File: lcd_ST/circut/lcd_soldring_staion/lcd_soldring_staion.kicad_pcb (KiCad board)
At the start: 2 copper layers, 41.7 x 41 mm, 35 parts, among them J2 Conn_01x05_Pin, J3 Conn_01x01_Pin, J4 Conn_01x01_Pin, J44 Screw_Terminal_01x02, J5 Conn_01x01_Pin, J6 Conn_01x01_Pin, J7 Conn_01x04_Pin, Q2 Si4162DY, SW1 SW_Push, U1 PIC16F15223T-I/SL, U2 L7805, U3 LM358

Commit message: done v0
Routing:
- net VPP: track 15.3 -> 15.8 mm

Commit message: V2_PCB EDITING
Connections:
- C4 pad 1: T+ -> T-
- C4 pad 2: T- -> T+
- C9 pad 1: c+ -> c-
- C9 pad 2: c- -> c+
- R10 pad 2: Net-(U3B--) -> Net-(U3B-+)
- R11 pad 1: Net-(U3B-+) -> Net-(U3B--)
- R2 pad 1: T+ -> T-
- R2 pad 2: Net-(U3A-+) -> Net-(U3A--)
- R3 pad 1: Net-(U3A-+) -> Net-(U3A--)
- R4 pad 1: T- -> T+
- R4 pad 2: Net-(U3A--) -> Net-(U3A-+)
- R5 pad 2: Net-(U3A--) -> Net-(U3A-+)
- R8 pad 1: c+ -> c-
- R8 pad 2: Net-(U3B-+) -> Net-(U3B--)
- R9 pad 1: c- -> c+
- R9 pad 2: Net-(U3B--) -> Net-(U3B-+)
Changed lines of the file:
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@@
 			(layers "B.Cu" "B.Mask" "B.Paste")
 			(roundrect_rratio 0.192308)
-			(net 19 "Net-(U3A--)")
+			(net 17 "Net-(U3A-+)")
 			(pintype "passive")
 		)
@@
 			(layers "B.Cu" "B.Mask" "B.Paste")
 			(roundrect_rratio 0.192308)
-			(net 5 "T-")
+			(net 6 "T+")
 			(pintype "passive")
 		)
@@
 			(layers "B.Cu" "B.Mask" "B.Paste")
 			(roundrect_rratio 0.192308)
-			(net 19 "Net-(U3A--)")
+			(net 17 "Net-(U3A-+)")
 			(pintype "passive")
 		)
@@
 			(layers "B.Cu" "B.Mask" "B.Paste")
 			(roundrect_rratio 0.192308)
-			(net 2 "c-")
+			(net 9 "c+")
 			(pintype "passive")
 		)
@@
 			(layers "B.Cu" "B.Mask" "B.Paste")
 			(roundrect_rratio 0.192308)
-			(net 22 "Net-(U3B--)")
+			(net 21 "Net-(U3B-+)")
 			(pintype "passive")
 		)
@@
 			(layers "B.Cu" "B.Mask" "B.Paste")
 			(roundrect_rratio 0.192308)
-			(net 6 "T+")
+			(net 5 "T-")
 			(pintype "passive")
 		)
@@
 			(layers "B.Cu" "B.Mask" "B.Paste")
 			(roundrect_rratio 0.192308)
-			(net 17 "Net-(U3A-+)")
+			(net 19 "Net-(U3A--)")
 			(pintype "passive")
 		)
@@
 			(layers "B.Cu" "B.Mask" "B.Paste")
 			(roundrect_rratio 0.192308)
-			(net 17 "Net-(U3A-+)")
+			(net 19 "Net-(U3A--)")
 			(pintype "passive")
 		)
@@
 			(layers "B.Cu" "B.Mask" "B.Paste")
 			(roundrect_rratio 0.188679)
-			(net 9 "c+")
+			(net 2 "c-")
 			(pintype "passive")
 		)
@@
 			(layers "B.Cu" "B.Mask" "B.Paste")
 			(roundrect_rratio 0.188679)
-			(net 2 "c-")
+			(net 9 "c+")
 			(pintype "passive")
 		)
@@
 			(layers "B.Cu" "B.Mask" "B.Paste")
 			(roundrect_rratio 0.192308)
-			(net 21 "Net-(U3B-+)")
+			(net 22 "Net-(U3B--)")
 			(pintype "passive")
 		)
@@
 			(layers "B.Cu" "B.Mask" "B.Paste")
 			(roundrect_rratio 0.192308)
-			(net 22 "Net-(U3B--)")
+			(net 21 "Net-(U3B-+)")
 			(pintype "passive")
 		)
@@
 			(layers "B.Cu" "B.Mask" "B.Paste")
 			(roundrect_rratio 0.188679)
-			(net 6 "T+")
+			(net 5 "T-")
 			(pintype "passive")
 		)
@@
 			(layers "B.Cu" "B.Mask" "B.Paste")
 			(roundrect_rratio 0.188679)
-			(net 5 "T-")
+			(net 6 "T+")
 			(pintype "passive")
 		)
@@
 			(layers "B.Cu" "B.Mask" "B.Paste")
 			(roundrect_rratio 0.192308)
-			(net 9 "c+")
+			(net 2 "c-")
 			(pintype "passive")
 		)
@@
 			(layers "B.Cu" "B.Mask" "B.Paste")
 			(roundrect_rratio 0.192308)
-			(net 21 "Net-(U3B-+)")
+			(net 22 "Net-(U3B--)")
 			(pintype "passive")
 		)

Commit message: pcb v2
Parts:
- added D1: LED, LED_SMD:LED_1210_3225Metric_Pad1.42x2.65mm_HandSolder, B.Cu at (119.4, 67.2)
- added J8: 01x04, Connector:01x04_fat_pins, F.Cu at (106.6, 64.1)
- added J9: Connector:01x04_fat_pins, Connector:01x04_fat_pins, F.Cu at (106.6, 72.1)
- added R14: 1K, Resistor_SMD:R_0805_2012Metric_Pad1.20x1.40mm_HandSolder, B.Cu at (120.1, 57.6)
- added R15: 1K, Resistor_SMD:R_0805_2012Metric_Pad1.20x1.40mm_HandSolder, B.Cu at (120.1, 60.6)
- added R16: 1K, Resistor_SMD:R_0805_2012Metric_Pad1.20x1.40mm_HandSolder, B.Cu at (120.1, 63.5)
- J7: footprint Connector:FanPinHeader_1x04_P2.54mm_Vertical -> Connector:01x04_fat_pins
- R1, R10, R11, R12, R2, R3, R4, R5, R6, R8, R9: footprint Resistor_SMD:R_1206_3216Metric_Pad1.30x1.75mm_HandSolder -> Resistor_SMD:R_0805_2012Metric_Pad1.20x1.40mm_HandSolder
- R13: footprint Resistor_SMD:R_1812_4532Metric_Pad1.30x3.40mm_HandSolder -> Resistor_SMD:R_0805_2012Metric_Pad1.20x1.40mm_HandSolder
- R7: value 1K -> 0.02
- moved J7 4.16 mm to (131.2, 82.8)
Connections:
- net PGC renamed B
- net PGD renamed A
- net temp_set renamed ClC
- U1 pad 11: unconnected-(U1-RA2-Pad11) -> TX
- U1 pad 6: unconnected-(U1-RC4-Pad6) -> Net-(U1-RC4)
- U1 pad 8: unconnected-(U1-RC2-Pad8) -> RX

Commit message: pcb v2
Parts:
- removed J9: Connector:01x04_fat_pins, Connector:01x04_fat_pins
- removed R15: 1K, Resistor_SMD:R_0805_2012Metric_Pad1.20x1.40mm_HandSolder
- removed RV1: R_Potentiometer, Potentiometer_THT:Potentiometer_ACP_CA9-H2,5_Horizontal
- J7: footprint Connector:01x04_fat_pins -> Connector:FanPinHeader_1x04_P2.54mm_Vertical
- J8: value 01x04 -> Conn_01x04_Pin; footprint Connector:01x04_fat_pins -> Connector:FanPinHeader_1x04_P2.54mm_Vertical
- R1: value 330 -> 50; footprint Resistor_SMD:R_0805_2012Metric_Pad1.20x1.40mm_HandSolder -> Resistor_THT:R_Axial_DIN0207_L6.3mm_D2.5mm_P7.62mm_Horizontal
- moved C5 11.9 mm to (153.4, 65.8), turned to 0 degrees
- moved R9 3.07 mm to (164.1, 82.8)
- moved R2 2.84 mm to (159.8, 62.9)
- moved R8 2.33 mm to (161.2, 82.8)
- moved R3 1.91 mm to (158.7, 66.2), turned to 180 degrees
- moved R4 1.90 mm to (162.0, 62.9)
- moved R5 0.63 mm to (162.8, 66.6)
- moved R6 0.59 mm to (157.5, 62.8)
- turned C4 to 0 degrees
- turned C9 to 0 degrees
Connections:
- D1 pad 1: c- -> unconnected-(D1-K-Pad1)
- R16 pad 2: Net-(U1-RC4) -> unconnected-(R16-Pad2)
- U1 pad 6: Net-(U1-RC4) -> unconnected-(U1-RC4-Pad6)
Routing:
- net c-: track 168.7 -> 125.5 mm
- net c+: track 17.6 -> 2.68 mm
- net TEMP: track 36.5 -> 27.3 mm
- net Net-(U3A-+): track 14.4 -> 5.82 mm
- net Net-(U3B-+): track 4.94 -> 10.7 mm
- net T-: track 5.47 -> 0.00 mm
- net T+: track 4.95 -> 0.00 mm
- net Net-(U3B--): track 10.6 -> 6.59 mm
- net heater: track 10.5 -> 8.59 mm
- net current: track 21.3 -> 22.5 mm
- net Net-(U3A--): track 5.27 -> 6.12 mm
- net Net-(R11-Pad2): track 5.40 -> 6.04 mm

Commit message: pcbing
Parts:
- removed J4: Conn_01x01_Pin, Connector_PinHeader_2.54mm:PinHeader_1x01_P2.54mm_Vertical
- removed R14: 1K, Resistor_SMD:R_0805_2012Metric_Pad1.20x1.40mm_HandSolder
- J7, J8: footprint Connector:FanPinHeader_1x04_P2.54mm_Vertical -> Connector:01x04_fat_pins
- U3: footprint Package_SO:SOIC-8_5.3x6.2mm_P1.27mm -> Package_SO:SOIC-8_3.9x4.9mm_P1.27mm
- moved J8 35.4 mm to (131.4, 89.2), turned to 90 degrees
- moved R1 4.90 mm to (145.9, 62.2)
- moved J7 3.90 mm to (131.4, 78.9)
- moved C6 1.76 mm to (152.3, 84.6)
- moved C1 1.47 mm to (136.0, 79.2), turned to -90 degrees
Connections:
- U1 pad 10: dat -> clk
- U1 pad 11: TX -> dat
- U1 pad 9: clk -> TX
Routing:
- net c-: track 125.5 -> 96.8 mm
- net VCC: track 66.8 -> 79.8 mm
- net RX: track 0.00 -> 11.8 mm
- net TX: track 0.00 -> 11.4 mm
- net +24V: track 17.2 -> 6.60 mm
- net Net-(U3B--): track 6.59 -> 7.62 mm
- net Net-(R11-Pad2): track 6.04 -> 7.06 mm
- net Net-(U3A--): track 6.12 -> 7.14 mm
- net Net-(U3A-+): track 5.82 -> 6.84 mm
- net Net-(R3-Pad2): track 6.61 -> 7.58 mm
- net Net-(U3B-+): track 10.7 -> 11.7 mm
- net clk: track 8.53 -> 7.98 mm
- added copper zone on B.Cu, net Net-(U2-IN)

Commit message: da
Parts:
- added J10: Conn_01x03_Pin, Connector:FanPinHeader_1x03_P2.54mm_Vertical, F.Cu at (153.6, 77.0)
- moved C6 0.13 mm to (152.2, 84.5)
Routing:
- net c-: track 96.8 -> 105.8 mm
- net ClC: track 17.6 -> 21.1 mm
- net VCC: track 79.8 -> 80.4 mm

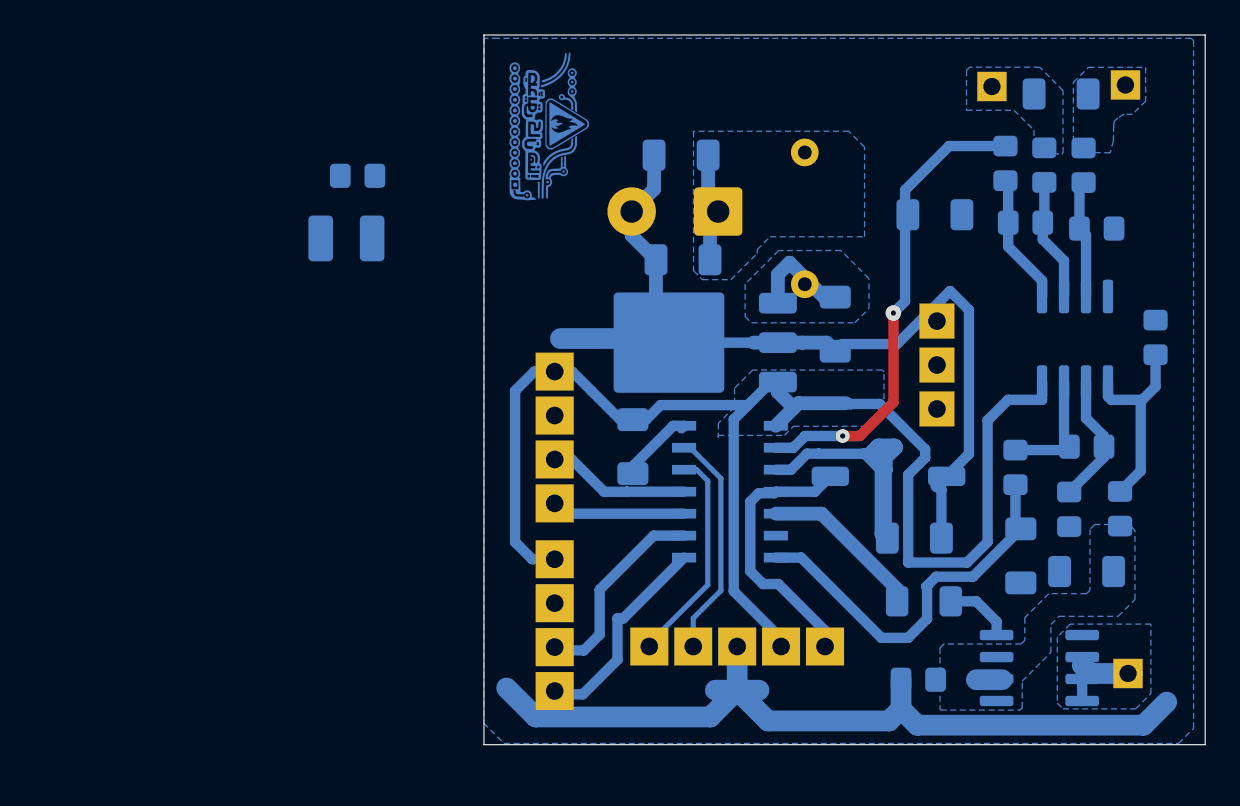
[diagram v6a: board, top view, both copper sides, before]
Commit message: Update lcd_soldring_staion.kicad_pcb
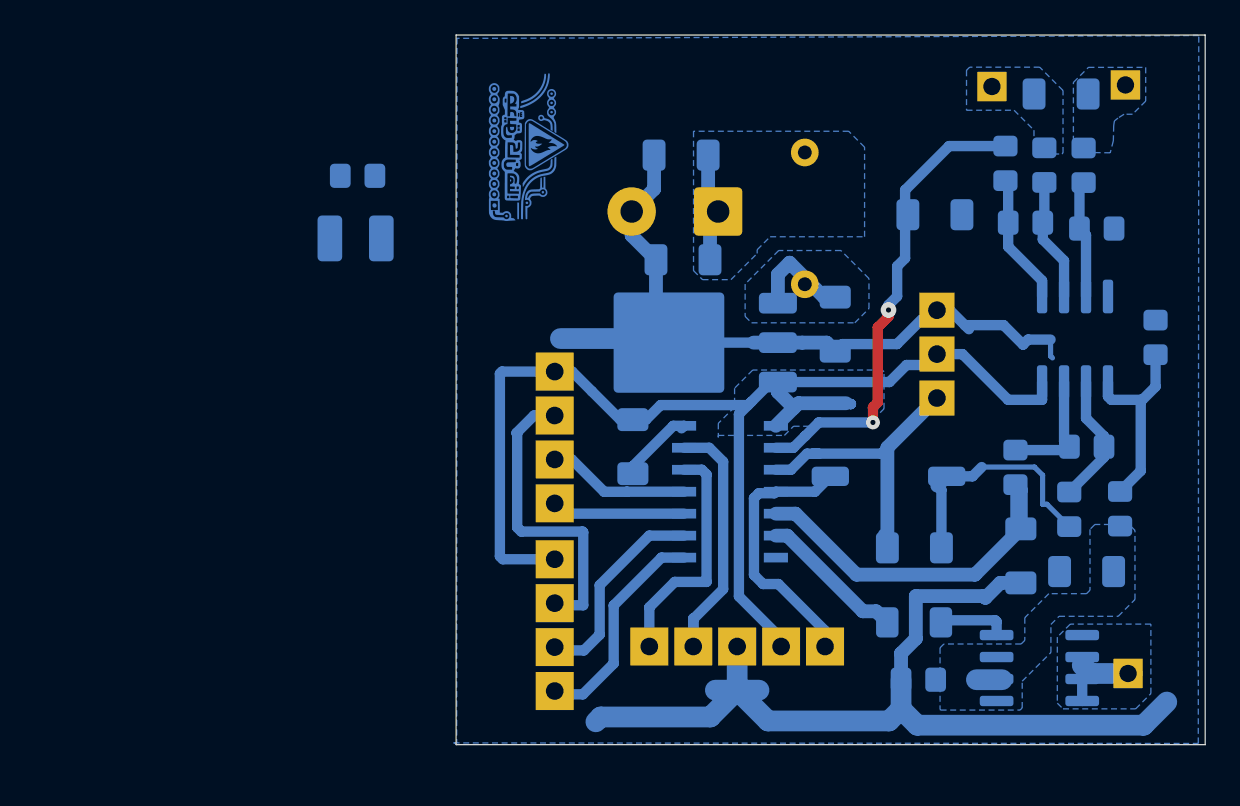
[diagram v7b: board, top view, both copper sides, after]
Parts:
- moved R7 1.34 mm to (152.2, 89.4)
- moved J10 0.63 mm to (153.6, 76.4)
- moved C6 0.56 mm to (152.2, 85.0)
- moved D1 0.53 mm to (119.9, 67.2), turned to 0 degrees
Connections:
- U1 pad 5: heater_gate -> current
- U1 pad 6: unconnected-(U1-RC4-Pad6) -> heater_gate
- U1 pad 7: current -> unconnected-(U1-RC3-Pad7)
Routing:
- net c-: track 105.8 -> 136.0 mm
- net VCC: track 80.4 -> 71.7 mm
- net A: track 13.2 -> 17.6 mm
- net ClC: track 21.1 -> 18.0 mm
- net B: track 12.6 -> 14.7 mm
- net heater_gate: track 9.52 -> 8.64 mm
- net RX: track 11.8 -> 12.4 mm
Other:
- board size 41.7 x 41 mm -> 43.3 x 41 mm

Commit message: h
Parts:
- removed D1: LED, LED_SMD:LED_1210_3225Metric_Pad1.42x2.65mm_HandSolder
- removed R16: 1K, Resistor_SMD:R_0805_2012Metric_Pad1.20x1.40mm_HandSolder
- moved SW1 0.87 mm to (151.6, 80.9)
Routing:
- net T-: track 0.00 -> 5.84 mm
- net A: track 17.6 -> 12.9 mm
- net B: track 14.7 -> 12.6 mm
- net Net-(U3B-+): track 11.7 -> 12.8 mm
- net current: track 22.1 -> 21.6 mm
- net c-: track 136.0 -> 135.5 mm
- net RX: track 12.4 -> 11.9 mm
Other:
- board size 43.3 x 41 mm -> 45 x 42.6 mm
